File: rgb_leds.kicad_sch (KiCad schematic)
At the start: 14 parts

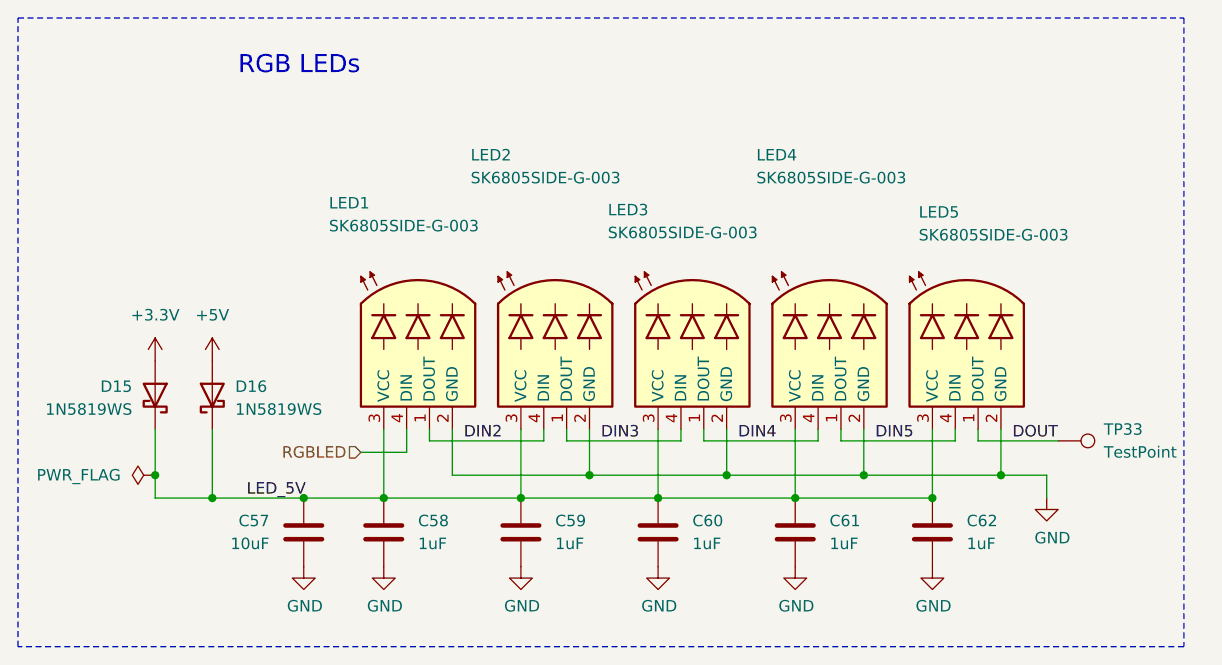
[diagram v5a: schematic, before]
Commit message: Final chores
- Reannotate components
- Improve USB2 connector skew matching
- Update sheet blocks
- Fix some diff-pair double-inversions
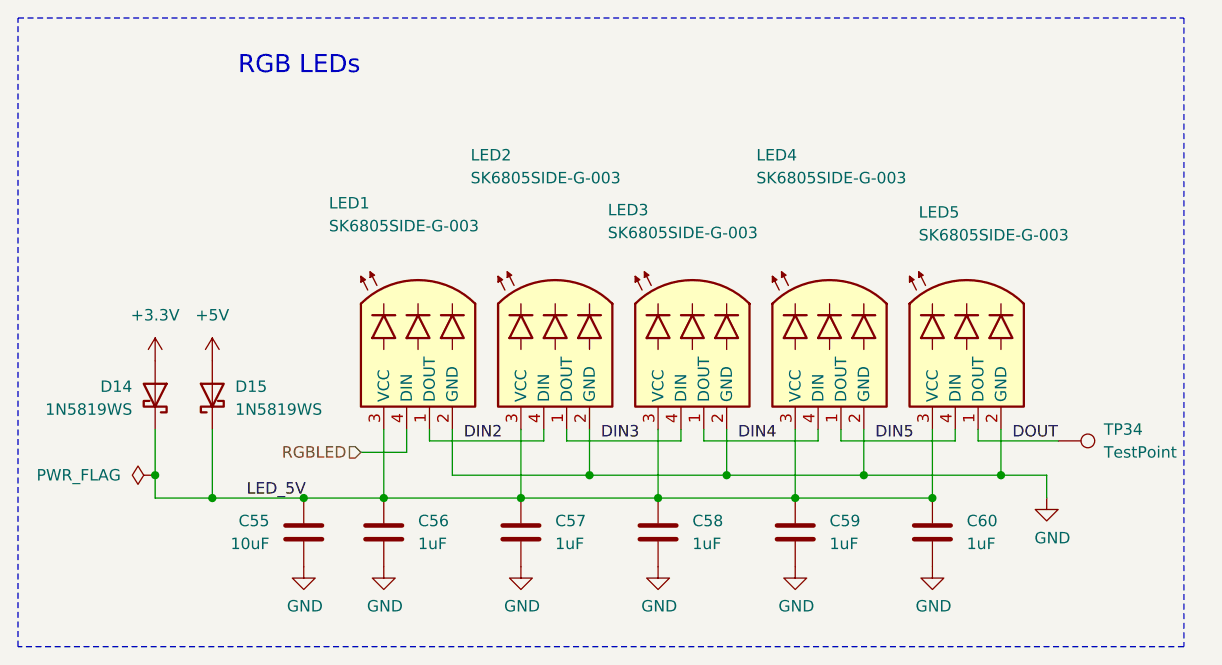
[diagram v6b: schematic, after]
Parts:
- renumbered C57 to C55, C58 to C56, C59 to C57, C60 to C58, C61 to C59, C62 to C60, D15 to D14, D16 to D15, TP33 to TP34
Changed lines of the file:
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@@
 	(title_block
 		(title "HALPI2")
-		(date "2025-03-27")
-		(rev "v0.2.0")
+		(date "2025-05-08")
+		(rev "v0.3.0")
 		(company "Hat Labs Oy")
 		(comment 1 "https://ohwr.org/cern_ohl_s_v2.pdf")
@@
 		(dnp no)
 		(fields_autoplaced yes)
-		(property "Reference" "C59"
+		(property "Reference" "C57"
 			(at 125.73 119.3799 0)
 			(effects
@@
 			(project "HALPI2"
 				(path "/abc482bd-3f17-4d35-80db-1da3dcdb5c27/850df4bf-e40a-4082-adc2-76804638b949/7441bc5f-8874-43c2-af8a-50459ea25028"
-					(reference "C59")
+					(reference "C57")
 					(unit 1)
 				)
@@
 		(on_board yes)
 		(dnp no)
-		(property "Reference" "#PWR078"
+		(property "Reference" "#PWR072"
 			(at 97.79 130.81 0)
 			(effects
@@
 			(project "HALPI2"
 				(path "/abc482bd-3f17-4d35-80db-1da3dcdb5c27/850df4bf-e40a-4082-adc2-76804638b949/7441bc5f-8874-43c2-af8a-50459ea25028"
-					(reference "#PWR078")
+					(reference "#PWR072")
 					(unit 1)
 				)
@@
 		(dnp no)
 		(fields_autoplaced yes)
-		(property "Reference" "C61"
+		(property "Reference" "C59"
 			(at 156.21 119.3799 0)
 			(effects
@@
 			(project "HALPI2"
 				(path "/abc482bd-3f17-4d35-80db-1da3dcdb5c27/850df4bf-e40a-4082-adc2-76804638b949/7441bc5f-8874-43c2-af8a-50459ea25028"
-					(reference "C61")
+					(reference "C59")
 					(unit 1)
 				)
@@
 		(dnp no)
 		(fields_autoplaced yes)
-		(property "Reference" "C60"
+		(property "Reference" "C58"
 			(at 140.97 119.3799 0)
 			(effects
@@
 			(project "HALPI2"
 				(path "/abc482bd-3f17-4d35-80db-1da3dcdb5c27/850df4bf-e40a-4082-adc2-76804638b949/7441bc5f-8874-43c2-af8a-50459ea25028"
-					(reference "C60")
+					(reference "C58")
 					(unit 1)
 				)
@@
 		(on_board yes)
 		(dnp no)
-		(property "Reference" "#PWR082"
+		(property "Reference" "#PWR076"
 			(at 152.4 130.81 0)
 			(effects
@@
 			(project "HALPI2"
 				(path "/abc482bd-3f17-4d35-80db-1da3dcdb5c27/850df4bf-e40a-4082-adc2-76804638b949/7441bc5f-8874-43c2-af8a-50459ea25028"
-					(reference "#PWR082")
+					(reference "#PWR076")
 					(unit 1)
 				)
@@
 		(dnp no)
 		(fields_autoplaced yes)
-		(property "Reference" "TP33"
+		(property "Reference" "TP34"
 			(at 186.69 109.2199 90)
 			(effects
@@
 			(project "HALPI2"
 				(path "/abc482bd-3f17-4d35-80db-1da3dcdb5c27/850df4bf-e40a-4082-adc2-76804638b949/7441bc5f-8874-43c2-af8a-50459ea25028"
-					(reference "TP33")
+					(reference "TP34")
 					(unit 1)
 				)
@@
 		(dnp no)
 		(fields_autoplaced yes)
-		(property "Reference" "#PWR076"
+		(property "Reference" "#PWR070"
 			(at 81.28 105.41 0)
 			(effects
@@
 			(project ""
 				(path "/abc482bd-3f17-4d35-80db-1da3dcdb5c27/850df4bf-e40a-4082-adc2-76804638b949/7441bc5f-8874-43c2-af8a-50459ea25028"
-					(reference "#PWR076")
+					(reference "#PWR070")
 					(unit 1)
 				)
@@
 		(on_board yes)
 		(dnp no)
-		(property "Reference" "#PWR079"
+		(property "Reference" "#PWR073"
 			(at 106.68 130.81 0)
 			(effects
@@
 			(project "HALPI2"
 				(path "/abc482bd-3f17-4d35-80db-1da3dcdb5c27/850df4bf-e40a-4082-adc2-76804638b949/7441bc5f-8874-43c2-af8a-50459ea25028"
-					(reference "#PWR079")
+					(reference "#PWR073")
 					(unit 1)
 				)
@@
 		(dnp no)
 		(fields_autoplaced yes)
-		(property "Reference" "D16"
+		(property "Reference" "D15"
 			(at 90.17 104.4574 90)
 			(effects
@@
 			(project ""
 				(path "/abc482bd-3f17-4d35-80db-1da3dcdb5c27/850df4bf-e40a-4082-adc2-76804638b949/7441bc5f-8874-43c2-af8a-50459ea25028"
-					(reference "D16")
+					(reference "D15")
 					(unit 1)
 				)
@@
 		(dnp no)
 		(fields_autoplaced yes)
-		(property "Reference" "#PWR077"
+		(property "Reference" "#PWR071"
 			(at 87.63 105.41 0)
 			(effects
@@
 			(project "HALPI2"
 				(path "/abc482bd-3f17-4d35-80db-1da3dcdb5c27/850df4bf-e40a-4082-adc2-76804638b949/7441bc5f-8874-43c2-af8a-50459ea25028"
-					(reference "#PWR077")
+					(reference "#PWR071")
 					(unit 1)
 				)
@@
 		(on_board yes)
 		(dnp no)
-		(property "Reference" "#PWR084"
+		(property "Reference" "#PWR078"
 			(at 180.34 123.19 0)
 			(effects
@@
 			(project "HALPI2"
 				(path "/abc482bd-3f17-4d35-80db-1da3dcdb5c27/850df4bf-e40a-4082-adc2-76804638b949/7441bc5f-8874-43c2-af8a-50459ea25028"
-					(reference "#PWR084")
+					(reference "#PWR078")
 					(unit 1)
 				)
@@
 		(on_board yes)
 		(dnp no)
-		(property "Reference" "C57"
+		(property "Reference" "C55"
 			(at 93.98 119.3799 0)
 			(effects
@@
 			(project "HALPI2"
 				(path "/abc482bd-3f17-4d35-80db-1da3dcdb5c27/850df4bf-e40a-4082-adc2-76804638b949/7441bc5f-8874-43c2-af8a-50459ea25028"
-					(reference "C57")
+					(reference "C55")
 					(unit 1)
 				)
@@
 		(on_board yes)
 		(dnp no)
-		(property "Reference" "#PWR083"
+		(property "Reference" "#PWR077"
 			(at 167.64 130.81 0)
 			(effects
@@
 			(project "HALPI2"
 				(path "/abc482bd-3f17-4d35-80db-1da3dcdb5c27/850df4bf-e40a-4082-adc2-76804638b949/7441bc5f-8874-43c2-af8a-50459ea25028"
-					(reference "#PWR083")
+					(reference "#PWR077")
 					(unit 1)
 				)
@@
 		(on_board yes)
 		(dnp no)
-		(property "Reference" "#PWR081"
+		(property "Reference" "#PWR075"
 			(at 137.16 130.81 0)
 			(effects
@@
 			(project "HALPI2"
 				(path "/abc482bd-3f17-4d35-80db-1da3dcdb5c27/850df4bf-e40a-4082-adc2-76804638b949/7441bc5f-8874-43c2-af8a-50459ea25028"
-					(reference "#PWR081")
+					(reference "#PWR075")
 					(unit 1)
 				)
@@
 		(on_board yes)
 		(dnp no)
-		(property "Reference" "D15"
+		(property "Reference" "D14"
 			(at 78.74 104.4574 90)
 			(effects
@@
 			(project "HALPI2"
 				(path "/abc482bd-3f17-4d35-80db-1da3dcdb5c27/850df4bf-e40a-4082-adc2-76804638b949/7441bc5f-8874-43c2-af8a-50459ea25028"
-					(reference "D15")
+					(reference "D14")
 					(unit 1)
 				)
@@
 		(dnp no)
 		(fields_autoplaced yes)
-		(property "Reference" "C62"
+		(property "Reference" "C60"
 			(at 171.45 119.3799 0)
 			(effects
@@
 			(project "HALPI2"
 				(path "/abc482bd-3f17-4d35-80db-1da3dcdb5c27/850df4bf-e40a-4082-adc2-76804638b949/7441bc5f-8874-43c2-af8a-50459ea25028"
-					(reference "C62")
+					(reference "C60")
 					(unit 1)
 				)
@@
 		(dnp no)
 		(fields_autoplaced yes)
-		(property "Reference" "C58"
+		(property "Reference" "C56"
 			(at 110.49 119.3799 0)
 			(effects
@@
 			(project "HALPI2"
 				(path "/abc482bd-3f17-4d35-80db-1da3dcdb5c27/850df4bf-e40a-4082-adc2-76804638b949/7441bc5f-8874-43c2-af8a-50459ea25028"
-					(reference "C58")
+					(reference "C56")
 					(unit 1)
 				)
@@
 		(on_board yes)
 		(dnp no)
-		(property "Reference" "#PWR080"
+		(property "Reference" "#PWR074"
 			(at 121.92 130.81 0)
 			(effects
@@
 			(project "HALPI2"
 				(path "/abc482bd-3f17-4d35-80db-1da3dcdb5c27/850df4bf-e40a-4082-adc2-76804638b949/7441bc5f-8874-43c2-af8a-50459ea25028"
-					(reference "#PWR080")
+					(reference "#PWR074")
 					(unit 1)
 				)
